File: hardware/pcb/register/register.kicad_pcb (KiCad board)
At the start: 2 copper layers, 31 parts, among them J1 IDC_02x08, J2 IDC_02x08, J3 01x04_F, U1 74HC245, U2 74HC173, U3 74HC173

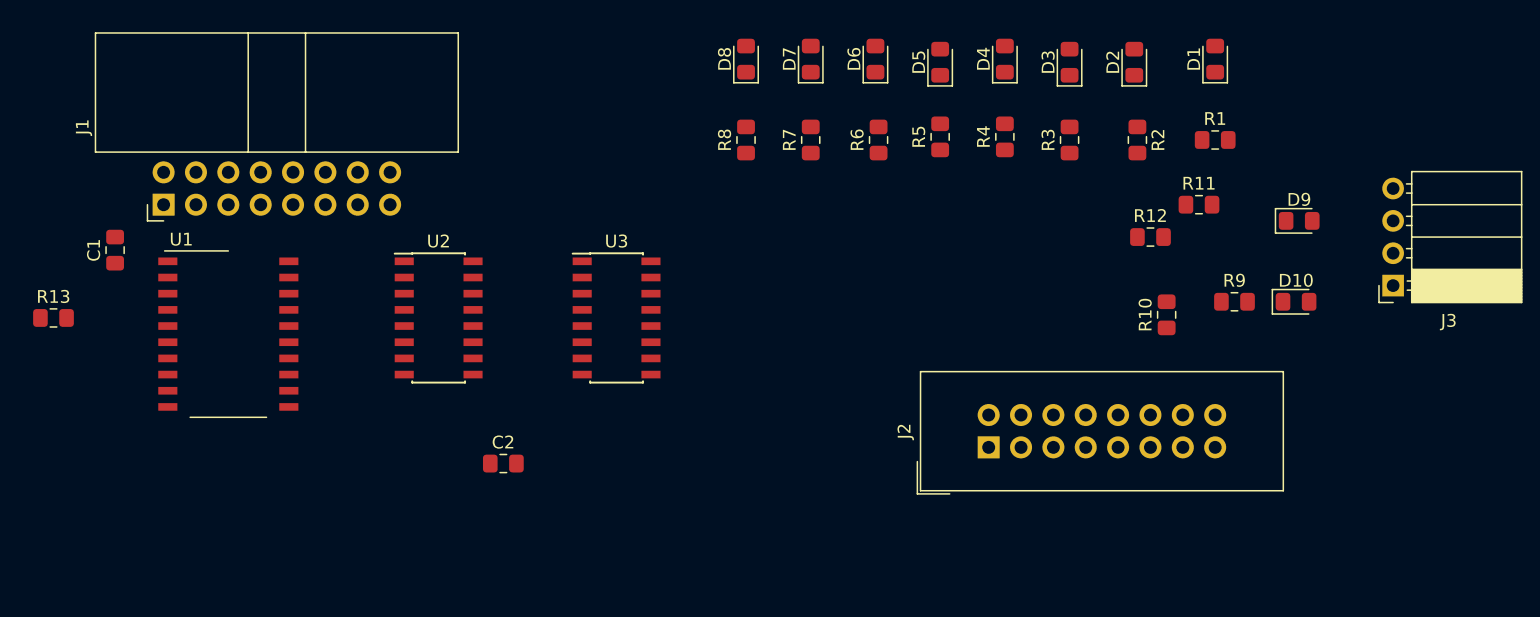
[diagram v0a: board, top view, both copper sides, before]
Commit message: Rearrange bus lines - MSB to the left
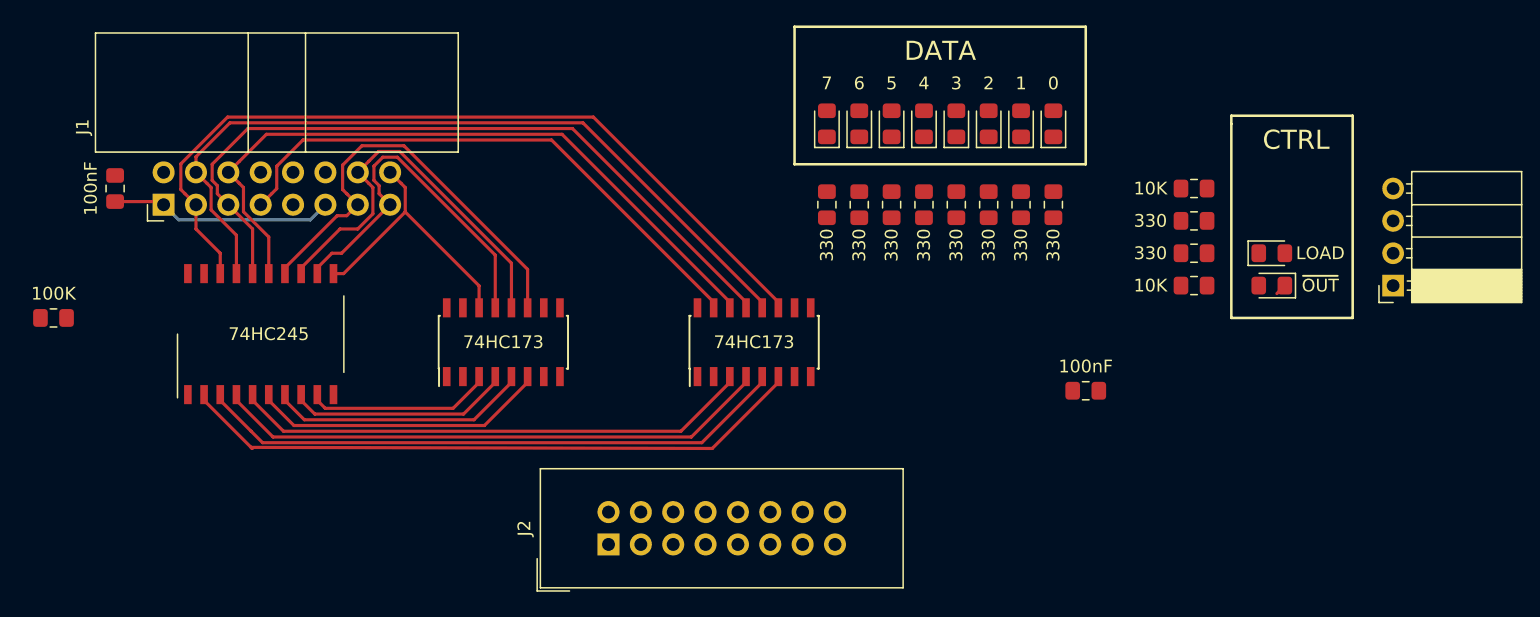
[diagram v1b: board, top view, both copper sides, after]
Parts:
- D1: value LED -> 0
- D10: value LED -> ~OUT~
- D2: value LED -> 1
- D3: value LED -> 2
- D4: value LED -> 3
- D5: value LED -> 4
- D6: value LED -> 5
- D7: value LED -> 6
- D8: value LED -> 7
- D9: value LED -> LOAD
- moved C2 46.1 mm to (175.3, 89.5)
- moved J2 30.8 mm to (137.8, 101.6)
- moved R1 13.7 mm to (172.7, 74.9), turned to 90 degrees
- moved D1 13.7 mm to (172.7, 68.6)
- moved U3 11.0 mm to (149.2, 85.7), turned to 90 degrees
- moved R2 10.5 mm to (170.2, 74.9), turned to 90 degrees
- moved D2 10.1 mm to (170.2, 68.6)
- moved R3 8.13 mm to (167.6, 74.9)
- moved R8 8.13 mm to (154.9, 74.9)
- moved D8 8.13 mm to (154.9, 68.6)
- moved D3 7.98 mm to (167.6, 68.6)
- moved R4 6.55 mm to (165.1, 74.9)
- moved R7 6.35 mm to (157.5, 74.9)
- moved D4 6.35 mm to (165.1, 68.6)
- moved D7 6.35 mm to (157.5, 68.6)
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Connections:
- U1 pad 11: BUS7 -> BUS0
- U1 pad 12: BUS6 -> BUS1
- U1 pad 13: BUS5 -> BUS2
- U1 pad 14: BUS4 -> BUS3
- U1 pad 15: BUS3 -> BUS4
- U1 pad 16: BUS2 -> BUS5
- U1 pad 17: BUS1 -> BUS6
- U1 pad 18: BUS0 -> BUS7
- U1 pad 2: TAP0 -> TAP7
- U1 pad 3: TAP1 -> TAP6
- U1 pad 4: TAP2 -> TAP5
- U1 pad 5: TAP3 -> TAP4
- U1 pad 6: TAP4 -> TAP3
- U1 pad 7: TAP5 -> TAP2
- U1 pad 8: TAP6 -> TAP1
- U1 pad 9: TAP7 -> TAP0
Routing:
- net BUS7: track 0.00 -> 64.8 mm
- net BUS6: track 0.00 -> 62.3 mm
- net BUS5: track 0.00 -> 59.1 mm
- net BUS4: track 0.00 -> 55.8 mm
- net TAP7: track 0.00 -> 49.9 mm
- net TAP6: track 0.00 -> 46.8 mm
- net RESET: track 0.00 -> 44.4 mm
- net TAP5: track 0.00 -> 43.9 mm
- net TAP4: track 0.00 -> 41.0 mm
- net BUS3: track 0.00 -> 34.0 mm
- net BUS2: track 0.00 -> 31.5 mm
- net BUS1: track 0.00 -> 28.9 mm
- net TAP3: track 0.00 -> 23.4 mm
- net BUS0: track 0.00 -> 21.2 mm
- net TAP2: track 0.00 -> 20.5 mm
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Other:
- board text added: "CTRL"
- board text added: "DATA"

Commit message: Board template (cleaned copy from ALU)
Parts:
- removed C1, C2: 100nF, Capacitor_SMD:C_0805_2012Metric_Pad1.15x1.40mm_HandSolder
- removed D10: ~OUT~, LED_SMD:LED_0805_2012Metric_Pad1.15x1.40mm_HandSolder
- removed D8: 7, LED_SMD:LED_0805_2012Metric_Pad1.15x1.40mm_HandSolder
- removed D9: LOAD, LED_SMD:LED_0805_2012Metric_Pad1.15x1.40mm_HandSolder
- removed R1, R10, R12, R2, R3, R4, R5, R6, R7, R8: 330, Resistor_SMD:R_0805_2012Metric_Pad1.15x1.40mm_HandSolder
- removed R11, R9: 10K, Resistor_SMD:R_0805_2012Metric_Pad1.15x1.40mm_HandSolder
- removed R13: 100K, Resistor_SMD:R_0805_2012Metric_Pad1.15x1.40mm_HandSolder
- removed U1: 74HC245, Package_SO:SO-20_12.8x7.5mm_P1.27mm
- removed U2, U3: 74HC173, Package_SO:SOIC-16_3.9x9.9mm_P1.27mm
- added D0: 0, LED_SMD:LED_0805_2012Metric_Pad1.15x1.40mm_HandSolder, F.Cu at (68.6, 50.7)
- added J4: Control, Connector_PinHeader_2.54mm:PinHeader_1x04_P2.54mm_Vertical, B.Cu at (36.8, 55.9)
- added J5: Flags, Connector_PinHeader_2.54mm:PinHeader_1x04_P2.54mm_Vertical, B.Cu at (57.1, 55.9)
- added J6: Power, Connector_PinHeader_2.54mm:PinHeader_2x02_P2.54mm_Vertical, B.Cu at (39.4, 40.6)
- D1: value 0 -> 1
- D2: value 1 -> 2
- D3: value 2 -> Result
- D4: value 3 -> 4
- D5: value 4 -> 5
- D6: value 5 -> 6
- D7: value 6 -> N
- J1: value IDC_02x08 -> BUS; footprint Connector_IDC:IDC-Header_2x08_P2.54mm_Horizontal -> Connector_PinHeader_2.54mm:PinHeader_1x08_P2.54mm_Vertical; moved to B.Cu
- J2: value IDC_02x08 -> Input A; footprint Connector_IDC:IDC-Header_2x08_P2.54mm_Vertical -> Connector_PinHeader_2.54mm:PinHeader_1x08_P2.54mm_Vertical; moved to B.Cu
- J3: value 01x04_F -> Input B; footprint Connector_PinSocket_2.54mm:PinSocket_1x04_P2.54mm_Horizontal -> Connector_PinHeader_2.54mm:PinHeader_1x08_P2.54mm_Vertical; moved to B.Cu
- moved J3 124.5 mm to (77.5, 55.9), turned to 270 degrees
- moved D1 107.5 mm to (66.7, 50.7), turned to 270 degrees
- moved D2 106.9 mm to (64.8, 50.7), turned to 270 degrees
- moved D3 106.3 mm to (62.9, 50.7), turned to 270 degrees
- moved D4 105.7 mm to (61.0, 50.7), turned to 270 degrees
- moved D5 105.0 mm to (59.1, 50.7), turned to 270 degrees
- moved D6 104.4 mm to (57.1, 50.7), turned to 270 degrees
- moved D7 103.8 mm to (55.2, 50.7), turned to 270 degrees
- moved J2 87.6 mm to (77.5, 38.1), turned to 270 degrees
- moved J1 64.8 mm to (49.5, 38.1), turned to 270 degrees
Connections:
- net Net-(J2-Pad1) renamed A7
- net Net-(J2-Pad7) renamed A1
- net Net-(J2-Pad8) renamed A0
- net Net-(J3-Pad3) renamed B5
- net Net-(J3-Pad4) renamed B4
- D1 pad 2: TAP0 -> SUM1
- D2 pad 2: TAP1 -> SUM2
- D3 pad 2: TAP2 -> SUM3
- D4 pad 2: TAP3 -> SUM4
- D5 pad 2: TAP4 -> SUM5
- D6 pad 2: TAP5 -> SUM6
- D7 pad 2: TAP6 -> SUM7
- J1 pad 1: VCC -> BUS7
- J1 pad 2: GND -> BUS6
- J1 pad 3: BUS7 -> BUS5
- J1 pad 4: BUS6 -> BUS4
- J1 pad 5: BUS5 -> BUS3
- J1 pad 6: BUS4 -> BUS2
- J1 pad 7: RESET -> BUS1
- J1 pad 8: ~RESET~ -> BUS0
- J2 pad 2: GND -> A6
- J2 pad 3: TAP7 -> A5
- J2 pad 4: TAP6 -> A4
- J2 pad 5: TAP5 -> A3
- J2 pad 6: TAP4 -> A2
- J3 pad 1: ~OUT~ -> B7
- J3 pad 2: LOAD -> B6
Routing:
- net BUS7: track 64.8 -> 0.80 mm
- net BUS6: track 62.3 -> 0.00 mm
- net BUS5: track 59.1 -> 0.00 mm
- net BUS4: track 55.8 -> 0.00 mm
- net TAP7: track 49.9 -> 0.00 mm
- net TAP6: track 46.8 -> 0.00 mm
- net RESET: track 44.4 -> 0.00 mm
- net TAP5: track 43.9 -> 0.00 mm
- net TAP4: track 41.0 -> 0.00 mm
- net BUS3: track 34.0 -> 0.00 mm
- net BUS2: track 31.5 -> 0.00 mm
- net BUS1: track 28.9 -> 0.00 mm
- net TAP3: track 23.4 -> 0.00 mm
- net BUS0: track 21.2 -> 0.00 mm
- net TAP2: track 20.5 -> 0.00 mm
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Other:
- board outline added: 62.2 x 21.6 mm
- rule pad_to_mask_clearance: 0.051 -> 0
- board text added: "+ Power -"
- board text added: "A 7-0"
- board text added: "B 7-0"
- board text added: "Bus 7-0"
- board text added: "CI V CO Z"
- board text added: "Control"
- board text added: "Flags"
- board text added: "Register v1.0"
- board text added: "Velko 2020"
- board text added: "~OUT~ SUB / /"
- board text removed: "CTRL"
- board text removed: "DATA"

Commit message: Renamed references to match schematic
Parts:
- renumbered D0 to D1, D1 to D2, D2 to D3, D3 to D4, D4 to D5, D5 to D6, D6 to D7, D7 to D8, J4 to J2, J5 to J3, J6 to J4, J2 to J5, J3 to J6
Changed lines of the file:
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@@
     (tags "LED handsolder")
     (attr smd)
-    (fp_text reference D0 (at 2.54 0 270) (layer F.Fab) hide
+    (fp_text reference D1 (at 2.54 0 270) (layer F.Fab) hide
       (effects (font (size 1 1) (thickness 0.15)))
     )
@@
     (tags "LED handsolder")
     (attr smd)
-    (fp_text reference D1 (at 2.54 0 90) (layer F.Fab) hide
+    (fp_text reference D2 (at 2.54 0 90) (layer F.Fab) hide
       (effects (font (size 1 1) (thickness 0.15)))
     )
@@
     (tags "LED handsolder")
     (attr smd)
-    (fp_text reference D2 (at 2.54 0 270) (layer F.Fab) hide
+    (fp_text reference D3 (at 2.54 0 270) (layer F.Fab) hide
       (effects (font (size 1 1) (thickness 0.15)))
     )
@@
     (tags "LED handsolder")
     (attr smd)
-    (fp_text reference D3 (at 2.54 0 270) (layer F.Fab) hide
+    (fp_text reference D4 (at 2.54 0 270) (layer F.Fab) hide
       (effects (font (size 1 1) (thickness 0.15)))
     )
@@
     (tags "LED handsolder")
     (attr smd)
-    (fp_text reference D4 (at 2.54 0 270) (layer F.Fab) hide
+    (fp_text reference D5 (at 2.54 0 270) (layer F.Fab) hide
       (effects (font (size 1 1) (thickness 0.15)))
     )
@@
     (tags "LED handsolder")
     (attr smd)
-    (fp_text reference D5 (at 2.54 0 270) (layer F.Fab) hide
+    (fp_text reference D6 (at 2.54 0 270) (layer F.Fab) hide
       (effects (font (size 1 1) (thickness 0.15)))
     )
@@
     (tags "LED handsolder")
     (attr smd)
-    (fp_text reference D6 (at 2.54 0 270) (layer F.Fab) hide
+    (fp_text reference D7 (at 2.54 0 270) (layer F.Fab) hide
       (effects (font (size 1 1) (thickness 0.15)))
     )
@@
     (tags "LED handsolder")
     (attr smd)
-    (fp_text reference D7 (at 2.54 0 270) (layer F.Fab) hide
+    (fp_text reference D8 (at 2.54 0 270) (layer F.Fab) hide
       (effects (font (size 1 1) (thickness 0.15)))
     )
@@
     (descr "Through hole straight pin header, 1x08, 2.54mm pitch, single row")
     (tags "Through hole pin header THT 1x08 2.54mm single row")
-    (fp_text reference J2 (at 0 2.33 270) (layer B.Fab) hide
+    (fp_text reference J5 (at 0 2.33 270) (layer B.Fab) hide
       (effects (font (size 1 1) (thickness 0.15)) (justify mirror))
     )
@@
     (descr "Through hole straight pin header, 1x08, 2.54mm pitch, single row")
     (tags "Through hole pin header THT 1x08 2.54mm single row")
-    (fp_text reference J3 (at 0 2.33 270) (layer B.Fab) hide
+    (fp_text reference J6 (at 0 2.33 270) (layer B.Fab) hide
       (effects (font (size 1 1) (thickness 0.15)) (justify mirror))
     )
@@
     (descr "Through hole straight pin header, 1x04, 2.54mm pitch, single row")
     (tags "Through hole pin header THT 1x04 2.54mm single row")
-    (fp_text reference J4 (at 0 2.33 270) (layer B.Fab) hide
+    (fp_text reference J2 (at 0 2.33 270) (layer B.Fab) hide
       (effects (font (size 1 1) (thickness 0.15)) (justify mirror))
     )
@@
     (descr "Through hole straight pin header, 1x04, 2.54mm pitch, single row")
     (tags "Through hole pin header THT 1x04 2.54mm single row")
-    (fp_text reference J5 (at 0 2.33 270) (layer B.Fab) hide
+    (fp_text reference J3 (at 0 2.33 270) (layer B.Fab) hide
       (effects (font (size 1 1) (thickness 0.15)) (justify mirror))
     )
@@
     (descr "Through hole straight pin header, 2x02, 2.54mm pitch, double rows")
     (tags "Through hole pin header THT 2x02 2.54mm double row")
-    (fp_text reference J6 (at 1.27 2.33 90) (layer B.Fab) hide
-      (effects (font (size 1 1) (thickness 0.15)) (justify mirror))
-    )
+    (fp_text reference J4 (at 1.27 2.33 90) (layer B.Fab) hide
+      (effects (font (size 1 1) (thickness 0.15)) (justify mirror))
+    )

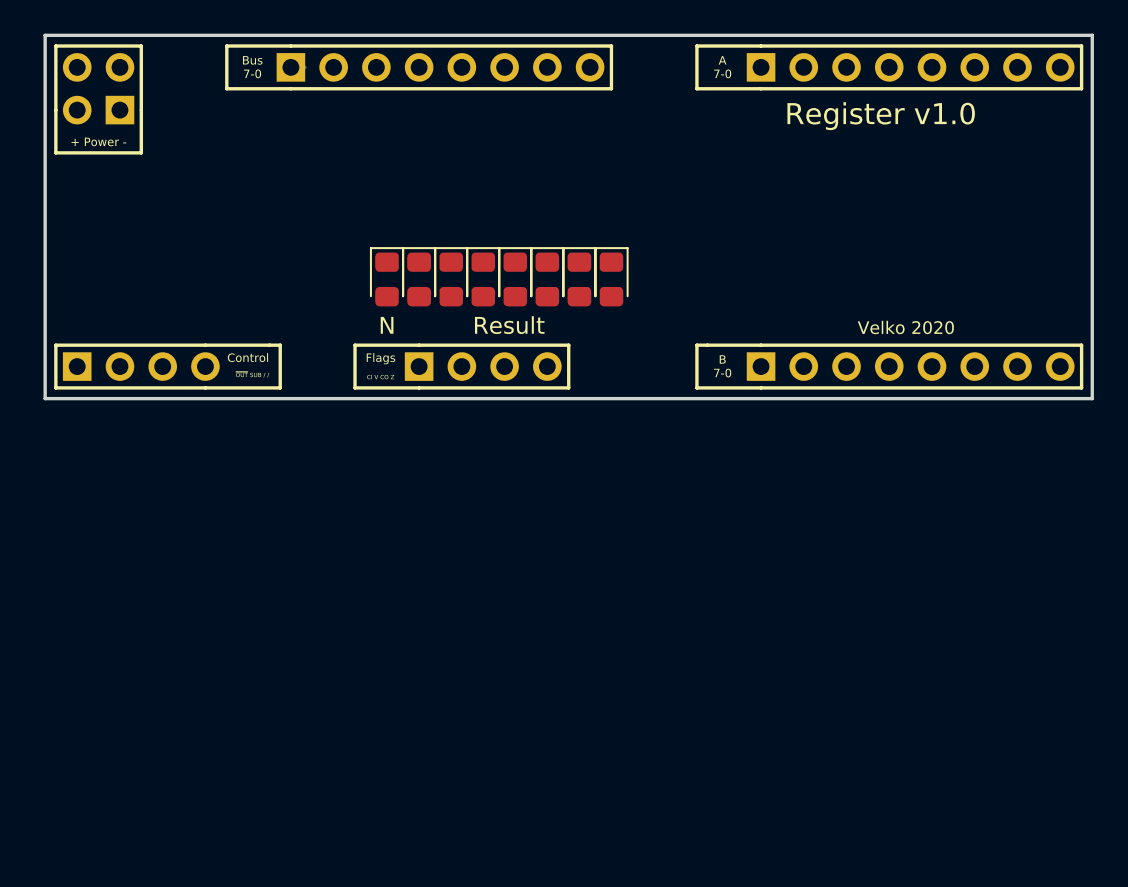
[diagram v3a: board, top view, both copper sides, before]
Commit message: Add footprints & import parts on PCB
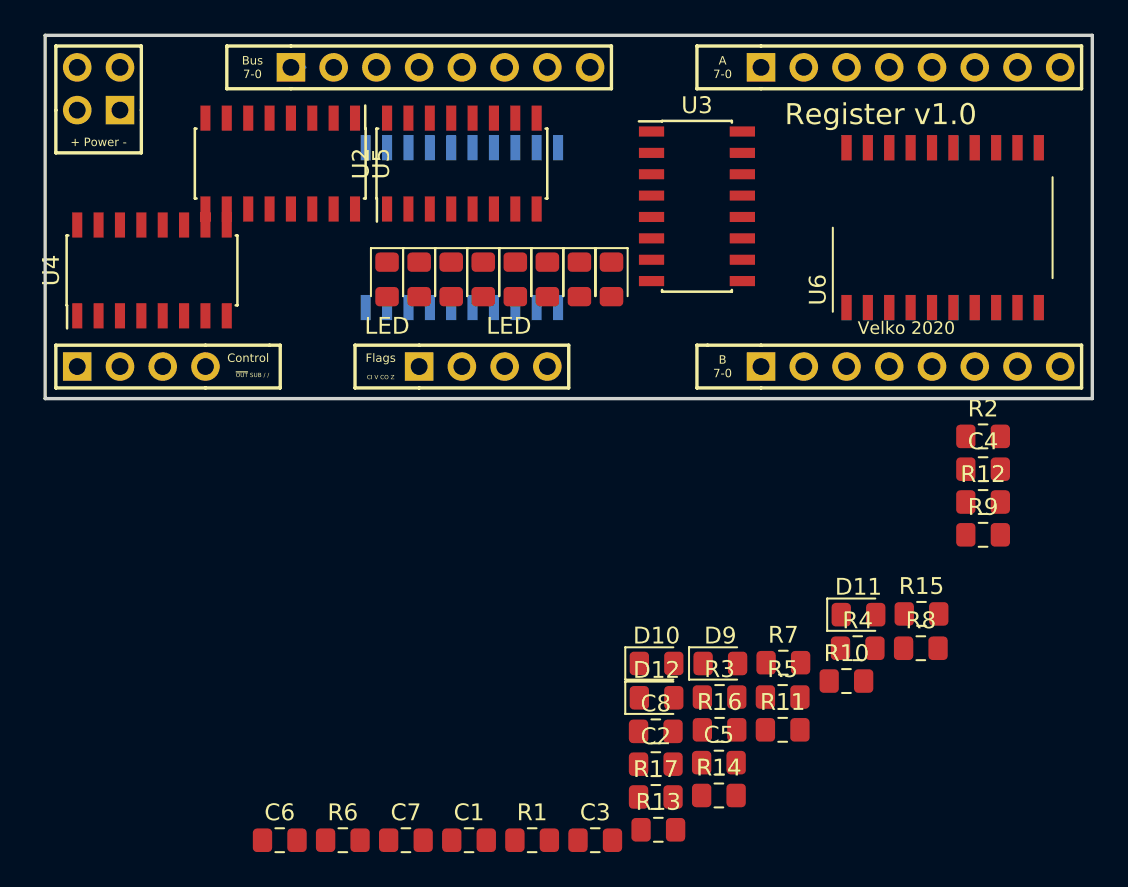
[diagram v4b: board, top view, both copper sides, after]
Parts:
- added C1: 100nF, Capacitor_SMD:C_0805_2012Metric_Pad1.15x1.40mm_HandSolder, F.Cu at (60.1, 84.0)
- added C2: 10µF, Capacitor_SMD:C_0805_2012Metric_Pad1.15x1.40mm_HandSolder, F.Cu at (71.2, 79.5)
- added C3: 100nF, Capacitor_SMD:C_0805_2012Metric_Pad1.15x1.40mm_HandSolder, F.Cu at (67.6, 84.0)
- added C4: 100nF, Capacitor_SMD:C_0805_2012Metric_Pad1.15x1.40mm_HandSolder, F.Cu at (90.7, 62.0)
- added C5: 100nF, Capacitor_SMD:C_0805_2012Metric_Pad1.15x1.40mm_HandSolder, F.Cu at (75.0, 79.4)
- added C6: 100nF, Capacitor_SMD:C_0805_2012Metric_Pad1.15x1.40mm_HandSolder, F.Cu at (48.9, 84.0)
- added C7: 100nF, Capacitor_SMD:C_0805_2012Metric_Pad1.15x1.40mm_HandSolder, F.Cu at (56.4, 84.0)
- added C8: 100nF, Capacitor_SMD:C_0805_2012Metric_Pad1.15x1.40mm_HandSolder, F.Cu at (71.2, 77.6)
- added D10: LED, LED_SMD:LED_0805_2012Metric_Pad1.15x1.40mm_HandSolder, F.Cu at (71.3, 73.5)
- added D11: LED, LED_SMD:LED_0805_2012Metric_Pad1.15x1.40mm_HandSolder, F.Cu at (83.3, 70.6)
- added D12: LED, LED_SMD:LED_0805_2012Metric_Pad1.15x1.40mm_HandSolder, F.Cu at (71.3, 75.6)
- added D9: LED, LED_SMD:LED_0805_2012Metric_Pad1.15x1.40mm_HandSolder, F.Cu at (75.1, 73.5)
- added R1: 10K, Resistor_SMD:R_0805_2012Metric_Pad1.15x1.40mm_HandSolder, F.Cu at (63.9, 84.0)
- added R10: 330, Resistor_SMD:R_0805_2012Metric_Pad1.15x1.40mm_HandSolder, F.Cu at (82.5, 74.6)
- added R11: 330, Resistor_SMD:R_0805_2012Metric_Pad1.15x1.40mm_HandSolder, F.Cu at (78.8, 77.5)
- added R12: 330, Resistor_SMD:R_0805_2012Metric_Pad1.15x1.40mm_HandSolder, F.Cu at (90.7, 63.9)
- added R13: 100K, Resistor_SMD:R_0805_2012Metric_Pad1.15x1.40mm_HandSolder, F.Cu at (71.4, 83.4)
- added R14: 330, Resistor_SMD:R_0805_2012Metric_Pad1.15x1.40mm_HandSolder, F.Cu at (75.0, 81.4)
- added R15: 330, Resistor_SMD:R_0805_2012Metric_Pad1.15x1.40mm_HandSolder, F.Cu at (87.0, 70.6)
- added R16: 330, Resistor_SMD:R_0805_2012Metric_Pad1.15x1.40mm_HandSolder, F.Cu at (75.0, 77.5)
- added R17: 330, Resistor_SMD:R_0805_2012Metric_Pad1.15x1.40mm_HandSolder, F.Cu at (71.2, 81.5)
- added R2: 10K, Resistor_SMD:R_0805_2012Metric_Pad1.15x1.40mm_HandSolder, F.Cu at (90.7, 60.0)
- added R3: 10K, Resistor_SMD:R_0805_2012Metric_Pad1.15x1.40mm_HandSolder, F.Cu at (75.0, 75.5)
- added R4: 10K, Resistor_SMD:R_0805_2012Metric_Pad1.15x1.40mm_HandSolder, F.Cu at (83.2, 72.6)
- added R5: 330, Resistor_SMD:R_0805_2012Metric_Pad1.15x1.40mm_HandSolder, F.Cu at (78.8, 75.5)
- added R6: 330, Resistor_SMD:R_0805_2012Metric_Pad1.15x1.40mm_HandSolder, F.Cu at (52.6, 84.0)
- added R7: 330, Resistor_SMD:R_0805_2012Metric_Pad1.15x1.40mm_HandSolder, F.Cu at (78.8, 73.5)
- added R8: 330, Resistor_SMD:R_0805_2012Metric_Pad1.15x1.40mm_HandSolder, F.Cu at (87.0, 72.6)
- added R9: 330, Resistor_SMD:R_0805_2012Metric_Pad1.15x1.40mm_HandSolder, F.Cu at (90.7, 65.9)
- added U1: 74HC245, Package_SO:SO-20_12.8x7.5mm_P1.27mm, B.Cu at (59.7, 47.6)
- added U2: 74HC173, Package_SO:SOIC-16_3.9x9.9mm_P1.27mm, F.Cu at (59.7, 43.8)
- added U3: 74HC173, Package_SO:SOIC-16_3.9x9.9mm_P1.27mm, F.Cu at (73.7, 46.4)
- added U4: 74HC173, Package_SO:SOIC-16_3.9x9.9mm_P1.27mm, F.Cu at (41.3, 50.2)
- added U5: 74HC173, Package_SO:SOIC-16_3.9x9.9mm_P1.27mm, F.Cu at (48.9, 43.8)
- added U6: 74HC245, Package_SO:SO-20_12.8x7.5mm_P1.27mm, F.Cu at (88.3, 47.6)
- added U7: 74HC245, Package_SO:SO-20_12.8x7.5mm_P1.27mm, B.Cu at (88.3, 47.6)
- D1: value 0 -> LED
- D2: value 1 -> LED
- D3: value 2 -> LED
- D4: value Result -> LED
- D5: value 4 -> LED
- D6: value 5 -> LED
- D7: value 6 -> LED
- D8: value N -> LED
- J1: value BUS -> Conn_01x08_Male
- J2: value Control -> Conn_01x04_Male
- J3: value Flags -> Conn_01x04_Male
- J4: value Power -> Conn_01x04_Male
- J5: value Input A -> Conn_01x08_Male
- J6: value Input B -> Conn_01x08_Male
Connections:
- net ZIN renamed Net-(J3-Pad4)
- D1 pad 2: SUM0 -> M0
- D2 pad 2: SUM1 -> M1
- D3 pad 2: SUM2 -> M2
- D4 pad 2: SUM3 -> M3
- D5 pad 2: SUM4 -> M4
- D6 pad 2: SUM5 -> M5
- D7 pad 2: SUM6 -> M6
- D8 pad 2: SUM7 -> M7
- J2 pad 1: ~OUT~ -> ~BUS_OUT~
- J2 pad 2: ADD_SUB -> LOAD
- J2 pad 3: Net-(J4-Pad3) -> ~A_OUT~
- J2 pad 4: Net-(J4-Pad4) -> ~B_OUT~
- J3 pad 1: CIN -> CLK
- J3 pad 2: OOUT -> ~CLK~
- J3 pad 3: COUT -> RESET
